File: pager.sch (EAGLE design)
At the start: 62 parts, among them Q1 25 MHz, Q2 SI2333DS, SW1 CHS-01A1, SW2 CHS-01A1, U1 VOCORE2SMD, U2 VOCORE2SMD, U3 XR22800IL, X1 52745-3090

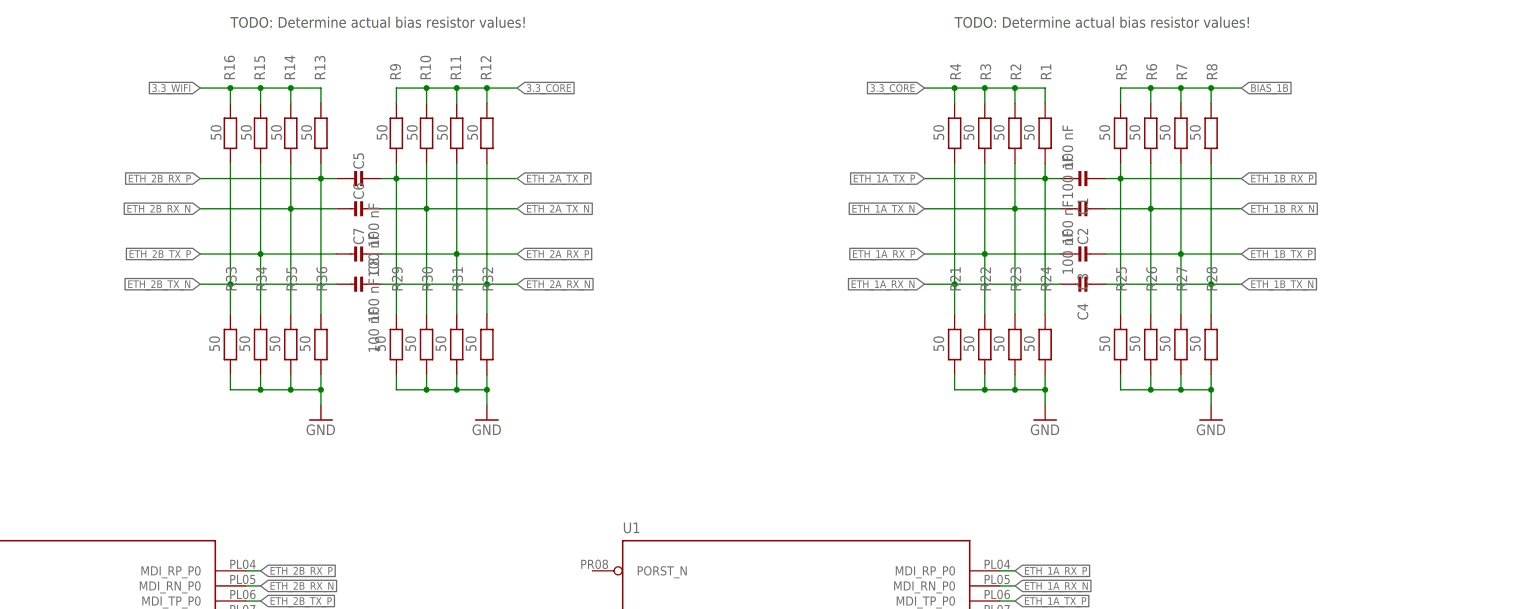
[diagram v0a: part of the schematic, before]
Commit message: cosmetic fixes to schematic
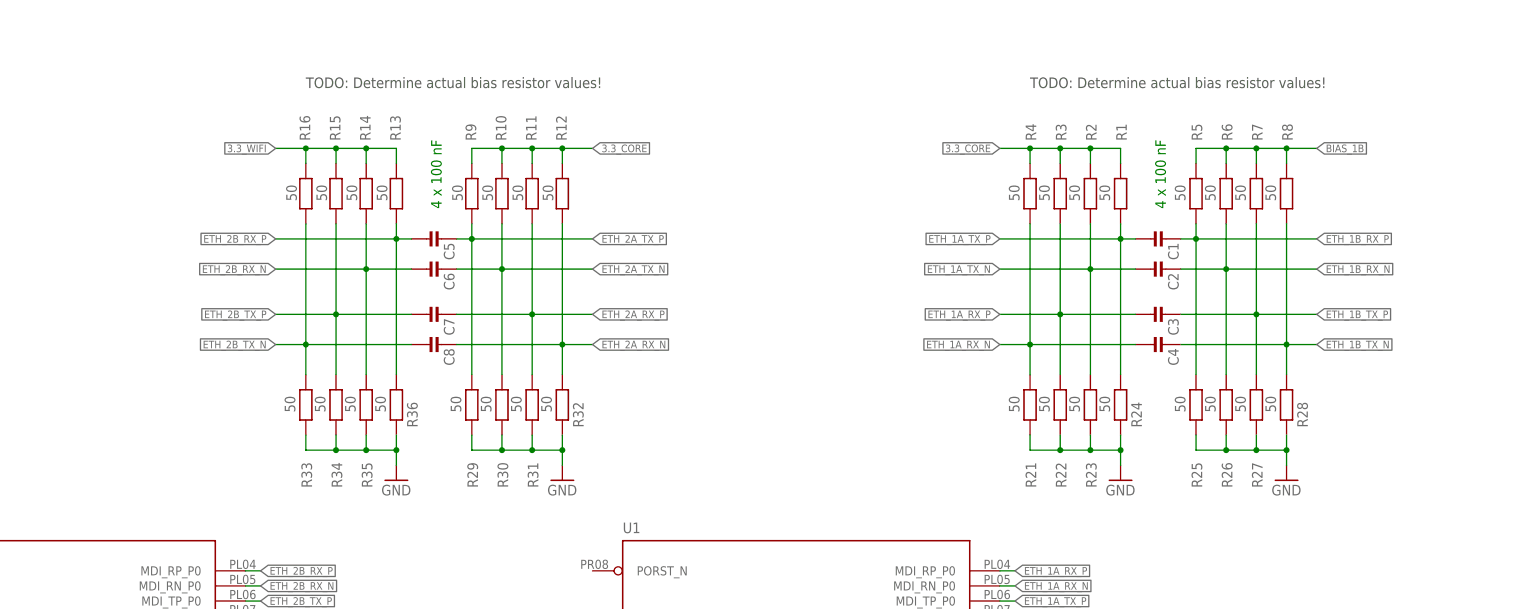
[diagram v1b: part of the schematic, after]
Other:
- note added: "4 x 100 nF"
- moved on the sheet: C1, C2, C3, C4, C5, C6, C7, C8, R1, R10, R11, R12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
